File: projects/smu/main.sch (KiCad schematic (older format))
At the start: 0 parts

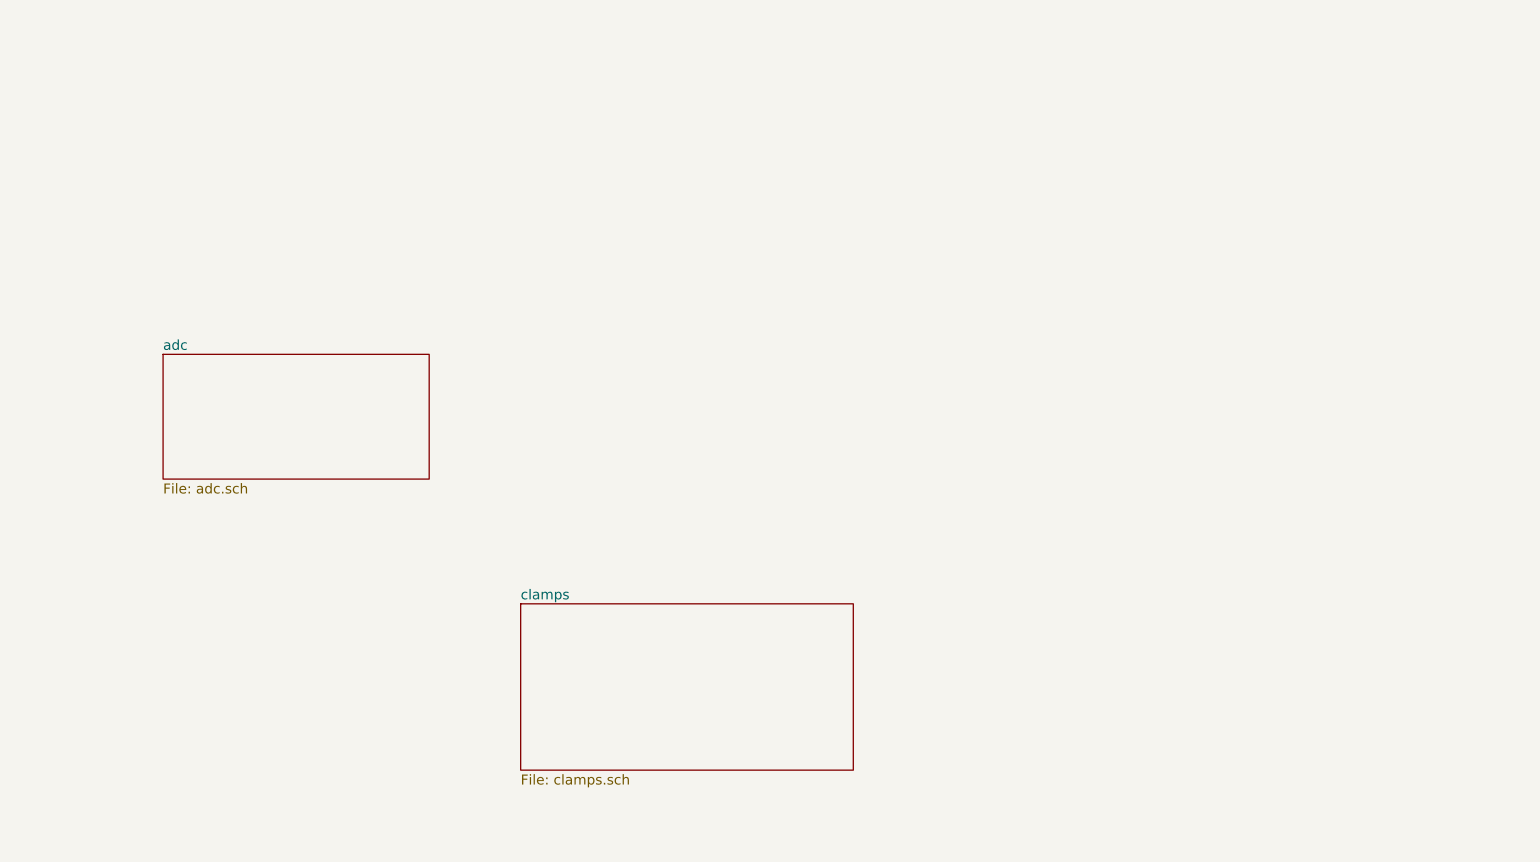
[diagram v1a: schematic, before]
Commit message: pulled out the connectors to the top sheet
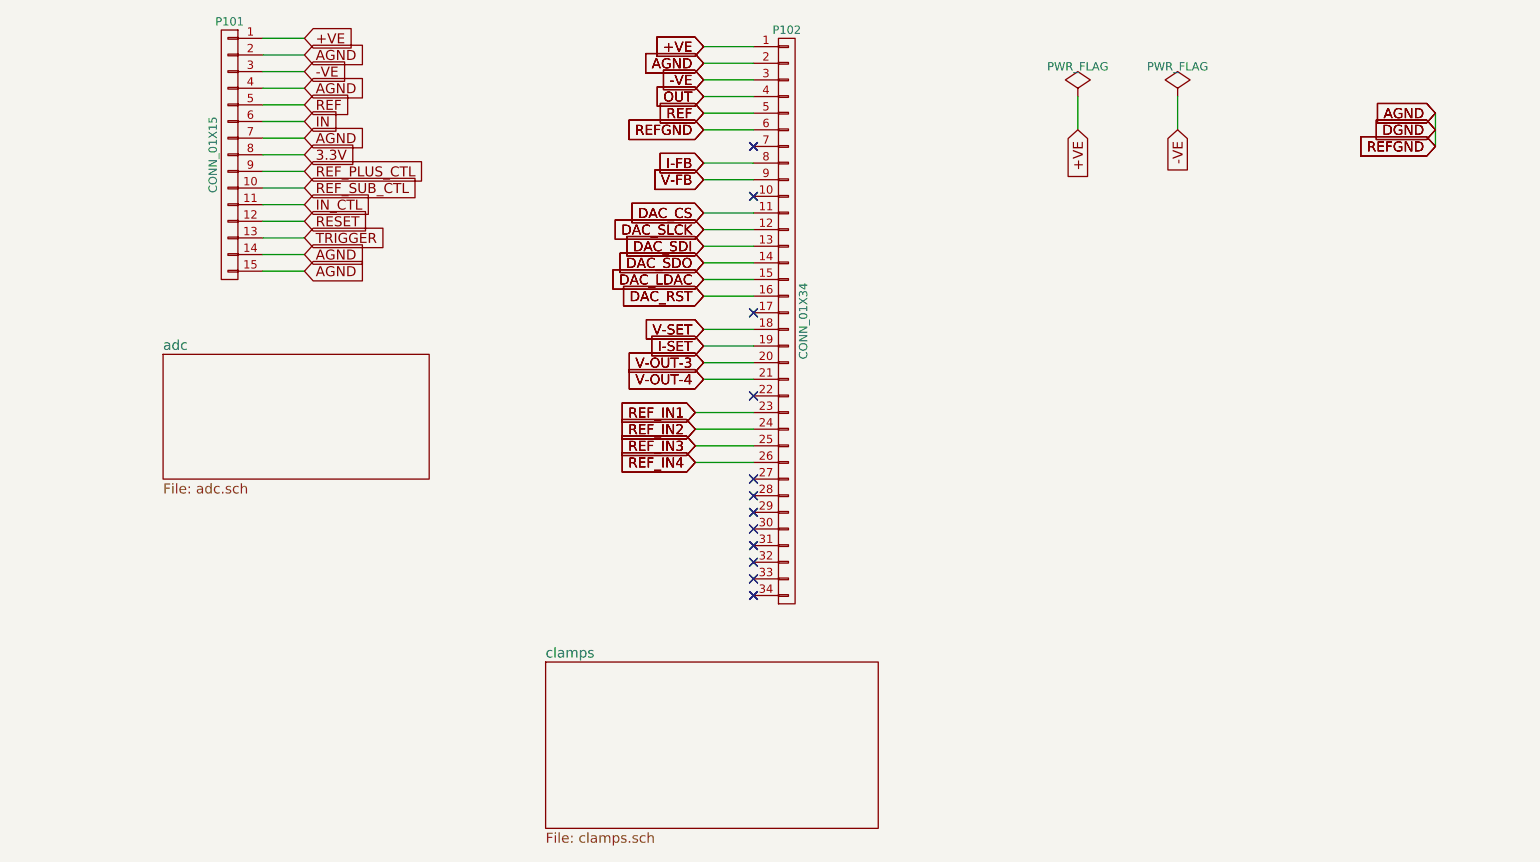
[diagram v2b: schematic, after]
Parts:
- added P101: CONN_01X15, Pin_Headers:Pin_Header_Straight_1x15, symbol CONN_01X15
- added P102: CONN_01X34, symbol CONN_01X34
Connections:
- new net +VE: P101.1 (P1), P102.1 (P1)
- new net -VE: P101.3 (P3), P102.3 (P3)
- new net 3.3V: P101.8 (P8)
- new net AGND: P101.14 (P14), P101.15 (P15), P101.2 (P2), P101.4 (P4), P101.7 (P7), P102.2 (P2), P102.6 (P6)
- new net DAC_CS: P102.11 (P11)
- new net DAC_LDAC: P102.15 (P15)
- new net DAC_RST: P102.16 (P16)
- new net DAC_SDI: P102.13 (P13)
- new net DAC_SDO: P102.14 (P14)
- new net DAC_SLCK: P102.12 (P12)
- new net I-FB: P102.8 (P8)
- new net I-SET: P102.19 (P19)
- new net IN: P101.6 (P6)
- new net IN_CTL: P101.11 (P11)
- new net OUT: P102.4 (P4)
- new net REF: P101.5 (P5), P102.5 (P5)
- new net REF_IN1: P102.23 (P23)
- new net REF_IN2: P102.24 (P24)
- new net REF_IN3: P102.25 (P25)
- new net REF_IN4: P102.26 (P26)
- new net REF_PLUS_CTL: P101.9 (P9)
- new net REF_SUB_CTL: P101.10 (P10)
- new net RESET: P101.12 (P12)
- new net TRIGGER: P101.13 (P13)
- new net V-FB: P102.9 (P9)
- new net V-OUT-3: P102.20 (P20)
- new net V-OUT-4: P102.21 (P21)
- new net V-SET: P102.18 (P18)
- no-connect marks 0 -> 24

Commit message: generate net and parts
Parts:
- P102: footprint (none) -> Pin_Headers:Pin_Header_Straight_1x34
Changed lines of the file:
@@
 F 0 "P102" H 5300 4400 50  0000 C CNN
 F 1 "CONN_01X34" V 5400 2650 50  0000 C CNN
-F 2 "" H 5300 2650 50  0000 C CNN
+F 2 "Pin_Headers:Pin_Header_Straight_1x34" H 5300 2650 50  0001 C CNN
 F 3 "" H 5300 2650 50  0000 C CNN
 	1    5300 2650

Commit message: do edges again
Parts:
- removed P102: CONN_01X34, Pin_Headers:Pin_Header_Straight_1x34, symbol CONN_01X34
- added P102: CONN_01X28, Pin_Headers:Pin_Header_Straight_1x28, symbol CONN_01X28
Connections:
- net +VE: now also P102.1 (P1)
- net -VE: now also P102.3 (P3)
- net AGND: now also P102.2 (P2), P102.6 (P6)
- net DAC_CS: now also P102.11 (P11)
- net DAC_LDAC: now also P102.15 (P15)
- net DAC_RST: now also P102.16 (P16)
- net DAC_SDI: now also P102.13 (P13)
- net DAC_SDO: now also P102.14 (P14)
- net DAC_SLCK: now also P102.12 (P12)
- net I-FB: now also P102.8 (P8)
- net I-SET: now also P102.19 (P19)
- net OUT: now also P102.4 (P4)
- net REF: now also P102.5 (P5)
- net REF_IN1: now also P102.23 (P23)
- net REF_IN2: now also P102.24 (P24)
- net V-FB: now also P102.9 (P9)
- net V-OUT-3: now also P102.20 (P20)
- net V-OUT-4: now also P102.21 (P21)
- net V-SET: now also P102.18 (P18)
- no-connect marks 24 -> 8
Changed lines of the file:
@@
 Wire Wire Line
 	2400 2350 2150 2350
-Text GLabel 4800 1000 0    60   Input ~ 0
-+VE
-Text GLabel 4800 1200 0    60   Input ~ 0
--VE
-Text GLabel 4800 1100 0    60   Input ~ 0
-AGND
-Text GLabel 4800 1400 0    60   Input ~ 0
-REF
 Wire Wire Line
 	5100 1000 4800 1000
@@
 Wire Wire Line
 	5100 1300 4800 1300
-Text GLabel 4800 1700 0    60   Input ~ 0
-I-FB
-Text GLabel 4800 1300 0    60   Input ~ 0
-OUT
-NoConn ~ 5100 1900
-Text GLabel 4800 1800 0    60   Input ~ 0
-V-FB
 Wire Wire Line
 	4800 1400 5100 1400
@@
 Wire Wire Line
 	7650 1300 7650 1500
-Text GLabel 4800 2900 0    60   Input ~ 0
-V-OUT-3
-Text GLabel 4800 3000 0    60   Input ~ 0
-V-OUT-4
-Text GLabel 4800 2000 0    60   Input ~ 0
-DAC_CS
-Text GLabel 4800 2100 0    60   Input ~ 0
-DAC_SLCK
-Text GLabel 4800 2200 0    60   Input ~ 0
-DAC_SDI
-Text GLabel 4800 2300 0    60   Input ~ 0
-DAC_SDO
-Text GLabel 4800 2400 0    60   Input ~ 0
-DAC_LDAC
-Text GLabel 4800 2500 0    60   Input ~ 0
-DAC_RST
 Wire Wire Line
 	4800 2000 5100 2000
@@
 Wire Wire Line
 	4800 2800 5100 2800
-Text GLabel 4800 2700 0    60   Input ~ 0
-V-SET
-Text GLabel 4800 2800 0    60   Input ~ 0
-I-SET
 Wire Wire Line
 	4800 2900 5100 2900
 Wire Wire Line
 	4800 3000 5100 3000
-NoConn ~ 5100 1600
-NoConn ~ 5100 2600
-Text GLabel 4750 3200 0    60   Input ~ 0
-REF_IN1
-Text GLabel 4750 3300 0    60   Input ~ 0
-REF_IN2
-Text GLabel 4750 3400 0    60   Input ~ 0
-REF_IN3
-Text GLabel 4750 3500 0    60   Input ~ 0
-REF_IN4
 Wire Wire Line
 	4750 3200 5100 3200
 Wire Wire Line
 	4750 3300 5100 3300
-Wire Wire Line
-	4750 3400 5100 3400
-Wire Wire Line
-	4750 3500 5100 3500
-NoConn ~ 5100 3100
-NoConn ~ 5100 3600
-NoConn ~ 5100 3700
-NoConn ~ 5100 3800
-NoConn ~ 5100 3900
-NoConn ~ 5100 4000
-NoConn ~ 5100 4100
-NoConn ~ 5100 4200
-NoConn ~ 5100 4300
-Text GLabel 4800 1500 0    60   Input ~ 0
-REFGND
 Wire Wire Line
 	4800 1500 5100 1500
@@
 NoConn ~ 5100 1600
 NoConn ~ 5100 2600
-$Comp
-L CONN_01X34 P102
-U 1 1 58A9E4F4
-P 5300 2650
-F 0 "P102" H 5300 4400 50  0000 C CNN
-F 1 "CONN_01X34" V 5400 2650 50  0000 C CNN
-F 2 "Pin_Headers:Pin_Header_Straight_1x34" H 5300 2650 50  0001 C CNN
-F 3 "" H 5300 2650 50  0000 C CNN
-	1    5300 2650
-	1    0    0    -1
-$EndComp
-Text GLabel 4750 3200 0    60   Input ~ 0
-REF_IN1
-Text GLabel 4750 3300 0    60   Input ~ 0
-REF_IN2
-Text GLabel 4750 3400 0    60   Input ~ 0
-REF_IN3
-Text GLabel 4750 3500 0    60   Input ~ 0
-REF_IN4
 NoConn ~ 5100 3100
 NoConn ~ 5100 3600
 NoConn ~ 5100 3700
-NoConn ~ 5100 3800
-NoConn ~ 5100 3900
-NoConn ~ 5100 4000
-NoConn ~ 5100 4100
-NoConn ~ 5100 4200
-NoConn ~ 5100 4300
 Text GLabel 4800 1500 0    60   Input ~ 0
 REFGND
+$Comp
+L CONN_01X28 P102
+U 1 1 58A96BF2
+P 5300 2350
+F 0 "P102" H 5300 3800 50  0000 C CNN
+F 1 "CONN_01X28" V 5400 2350 50  0000 C CNN
+F 2 "Pin_Headers:Pin_Header_Straight_1x28" H 5300 2350 50  0001 C CNN
+F 3 "" H 5300 2350 50  0000 C CNN
+	1    5300 2350
+	1    0    0    -1
+$EndComp
+Text GLabel 4750 3300 0    60   Input ~ 0
+REF_IN2
+Text GLabel 4750 3200 0    60   Input ~ 0
+REF_IN1
+NoConn ~ 5100 3400
+NoConn ~ 5100 3500
 $EndSCHEMATC

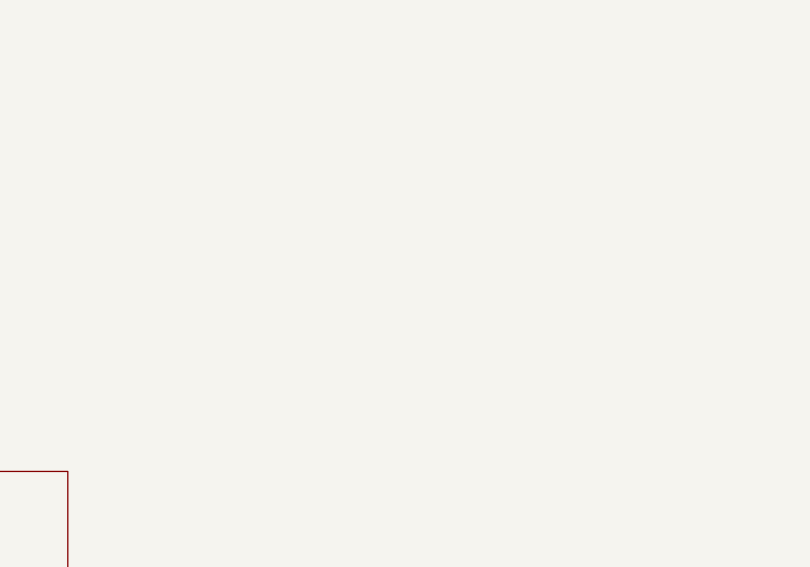
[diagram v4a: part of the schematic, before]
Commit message: add lt1021, remove net-tie
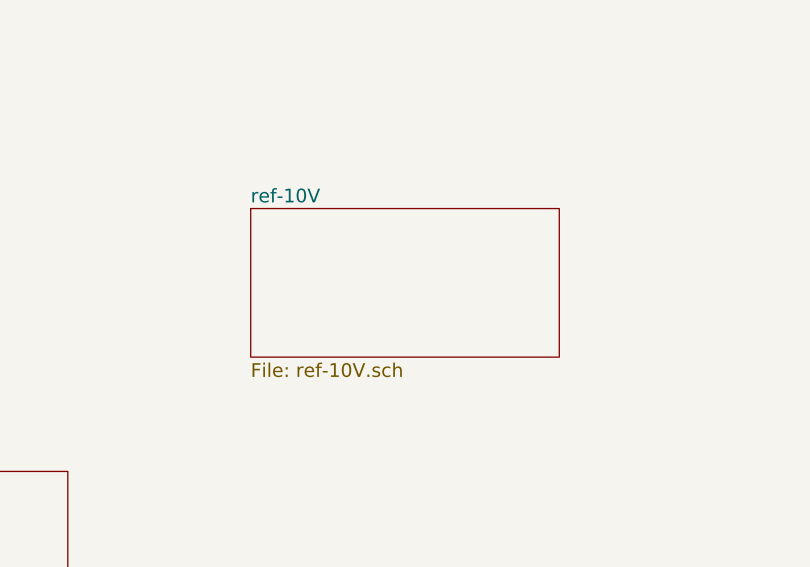
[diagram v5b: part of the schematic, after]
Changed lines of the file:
@@
 $Descr A4 11693 8268
 encoding utf-8
-Sheet 1 3
+Sheet 1 4
 Title ""
 Date ""
@@
 NoConn ~ 5100 3400
 NoConn ~ 5100 3500
+$Sheet
+S 6650 3550 1350 650
+U 58AD02DE
+F0 "ref-10V" 60
+F1 "ref-10V.sch" 60
+$EndSheet
 $EndSCHEMATC

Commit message: add power
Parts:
- added P103: CONN_01X15, Pin_Headers:Pin_Header_Straight_1x15, symbol CONN_01X15
- added P105: CONN_01X04, symbol CONN_01X04
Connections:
- net AGND: now also P103.2 (P2)
- new net PWR_+VE: P103.1 (P1)
- new net PWR_+VE_CTL: P105.1 (P1)
- new net PWR_-VE: P103.3 (P3)
- new net PWR_-VE_CTL: P105.2 (P2)
- no-connect marks 8 -> 22
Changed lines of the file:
@@
 $Descr A4 11693 8268
 encoding utf-8
-Sheet 1 4
+Sheet 1 5
 Title ""
 Date ""
@@
 F1 "ref-10V.sch" 60
 $EndSheet
+$Sheet
+S 8600 3200 1150 700
+U 58AD87F5
+F0 "power" 60
+F1 "power.sch" 60
+$EndSheet
+$Comp
+L CONN_01X15 P103
+U 1 1 58AE3540
+P 800 1650
+F 0 "P103" H 800 2450 50  0000 C CNN
+F 1 "CONN_01X15" V 900 1650 50  0000 C CNN
+F 2 "Pin_Headers:Pin_Header_Straight_1x15" H 800 1650 50  0001 C CNN
+F 3 "" H 800 1650 50  0000 C CNN
+	1    800  1650
+	-1   0    0    -1
+$EndComp
+Text GLabel 1000 950  2    60   Input ~ 0
+PWR_+VE
+Text GLabel 1000 1150 2    60   Input ~ 0
+PWR_-VE
+NoConn ~ 1000 1250
+NoConn ~ 1000 1350
+NoConn ~ 1000 1450
+NoConn ~ 1000 1550
+NoConn ~ 1000 1650
+NoConn ~ 1000 1750
+NoConn ~ 1000 1850
+NoConn ~ 1000 1950
+NoConn ~ 1000 2050
+NoConn ~ 1000 2150
+NoConn ~ 1000 2250
+NoConn ~ 1000 2350
+Text GLabel 1000 1050 2    60   Input ~ 0
+AGND
+$Comp
+L CONN_01X04 P105
+U 1 1 58AE3ABB
+P 3350 1200
+F 0 "P105" H 3350 1450 50  0000 C CNN
+F 1 "CONN_01X04" V 3450 1200 50  0000 C CNN
+F 2 "" H 3350 1200 50  0000 C CNN
+F 3 "" H 3350 1200 50  0000 C CNN
+	1    3350 1200
+	-1   0    0    -1
+$EndComp
+Text GLabel 3550 1050 2    60   Input ~ 0
+PWR_+VE_CTL
+Text GLabel 3550 1150 2    60   Input ~ 0
+PWR_-VE_CTL
+NoConn ~ 3550 1250
+NoConn ~ 3550 1350
 $EndSCHEMATC

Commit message: renaming pins
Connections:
- net IN renamed ADC_IN
- net IN_CTL renamed ADC_IN_CTL
- net REF_PLUS_CTL renamed ADC_PLUS_CTL
- net REF_SUB_CTL renamed ADC_MIN_CTL
- net RESET renamed ADC_RESET
- net TRIGGER renamed ADC_TRIGGER
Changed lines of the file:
@@
 REF
 Text GLabel 2400 1450 2    60   Input ~ 0
-IN
+ADC_IN
 Text GLabel 2400 1650 2    60   Input ~ 0
 3.3V
 Text GLabel 2400 1750 2    60   Input ~ 0
-REF_PLUS_CTL
+ADC_PLUS_CTL
 Text GLabel 2400 1850 2    60   Input ~ 0
-REF_SUB_CTL
+ADC_MIN_CTL
 Text GLabel 2400 1950 2    60   Input ~ 0
-IN_CTL
+ADC_IN_CTL
 Text GLabel 2400 2050 2    60   Input ~ 0
-RESET
+ADC_RESET
 $Comp
 L CONN_01X15 P101
@@
 AGND
 Text GLabel 2400 2150 2    60   Input ~ 0
-TRIGGER
+ADC_TRIGGER
 Wire Wire Line
 	2150 950  2400 950
